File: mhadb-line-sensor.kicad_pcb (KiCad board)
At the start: 2 copper layers, 100 x 20 mm, 106 parts, among them J1 TC2030, J2 Conn_01x04_Pin, J3 Conn_01x04, J4 Conn_01x04_Pin, SW1 SW_Push, SW2 SW_Push, SW3 SW_Push, SW4 SW_Push, U1 HT753-1, U10 QRE1113GR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

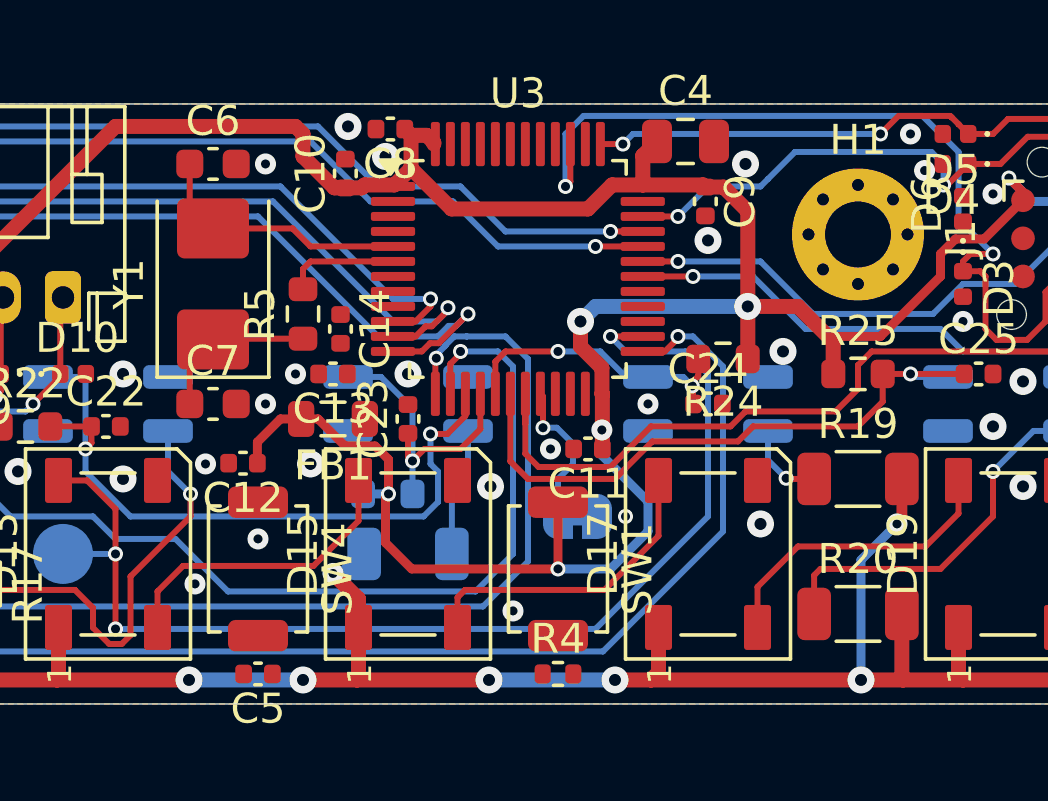
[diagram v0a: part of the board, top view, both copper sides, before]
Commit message: pcb: add BOOT and RST routing
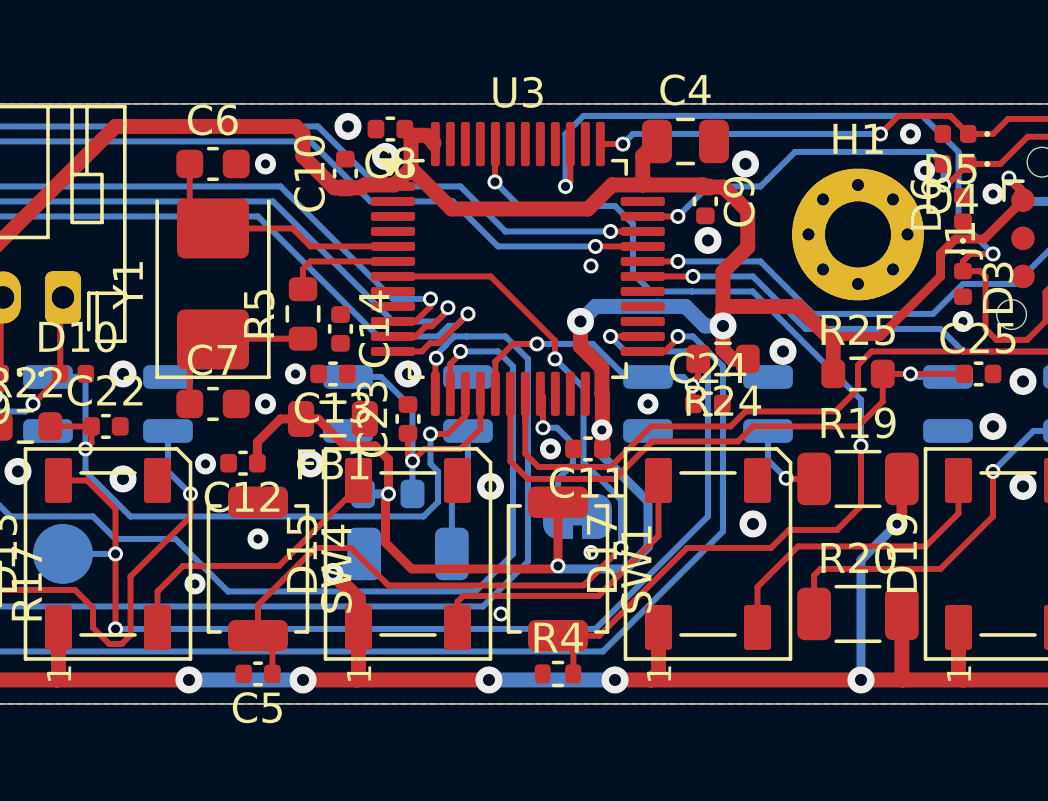
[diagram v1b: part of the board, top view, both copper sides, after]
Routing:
- net /BOOT: track 0.00 -> 34.4 mm, vias 0 -> 2
- net /NRST: track 0.00 -> 30.7 mm, vias 0 -> 2
- net +3V3: track 195.9 -> 198.0 mm
- net Net-(D13-DOUT): track 10.2 -> 9.55 mm
- net GND: vias 65 -> 66

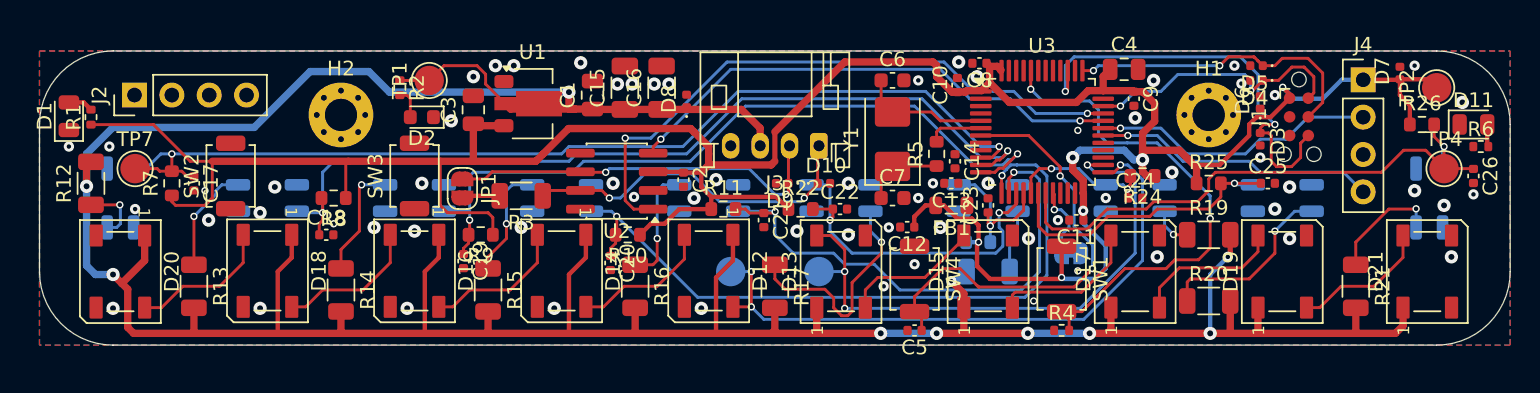
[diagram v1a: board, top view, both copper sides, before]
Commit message: pcb: add tag connect RST and CAN status led routing
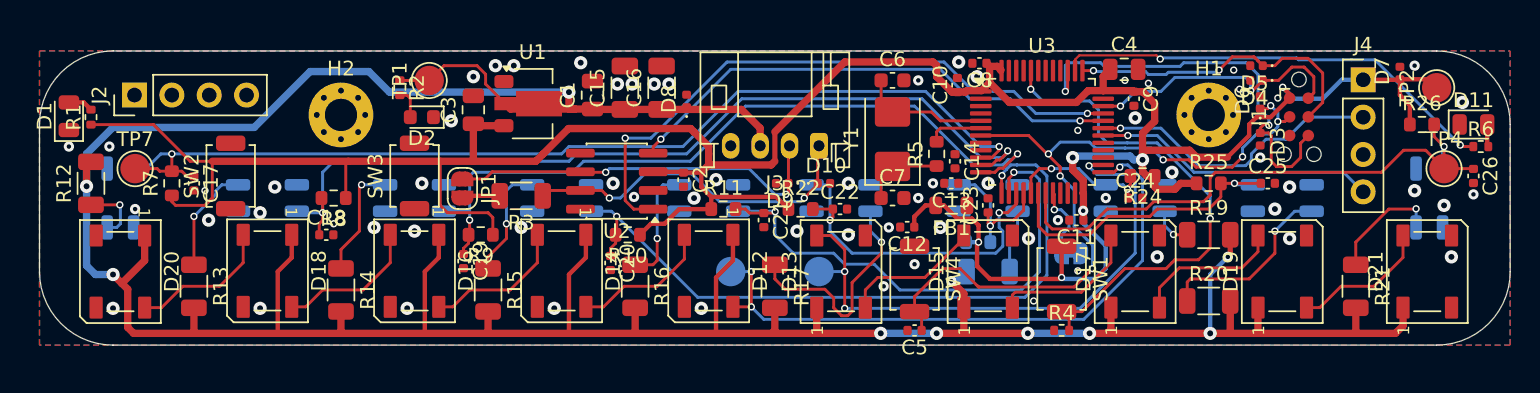
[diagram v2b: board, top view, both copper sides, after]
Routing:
- net Net-(U3-PA15): track 0.00 -> 30.6 mm, vias 0 -> 2
- net /NRST: track 30.7 -> 52.2 mm, vias 2 -> 7
- net +3V3: track 198.0 -> 199.9 mm
- net /U0RXD: track 19.4 -> 20.3 mm
- net /SWO: track 29.1 -> 28.4 mm
- net GND: vias 66 -> 67

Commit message: pcb: add btns routing
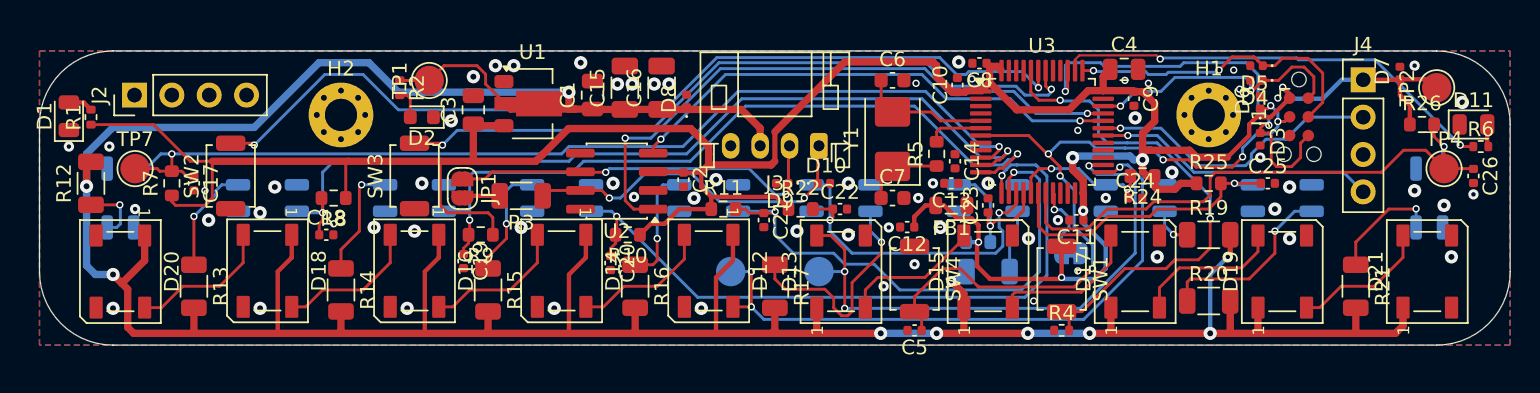
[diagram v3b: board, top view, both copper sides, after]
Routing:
- net /BTN1: track 0.00 -> 61.6 mm, vias 0 -> 2
- net /BTN2: track 0.00 -> 48.4 mm, vias 0 -> 2

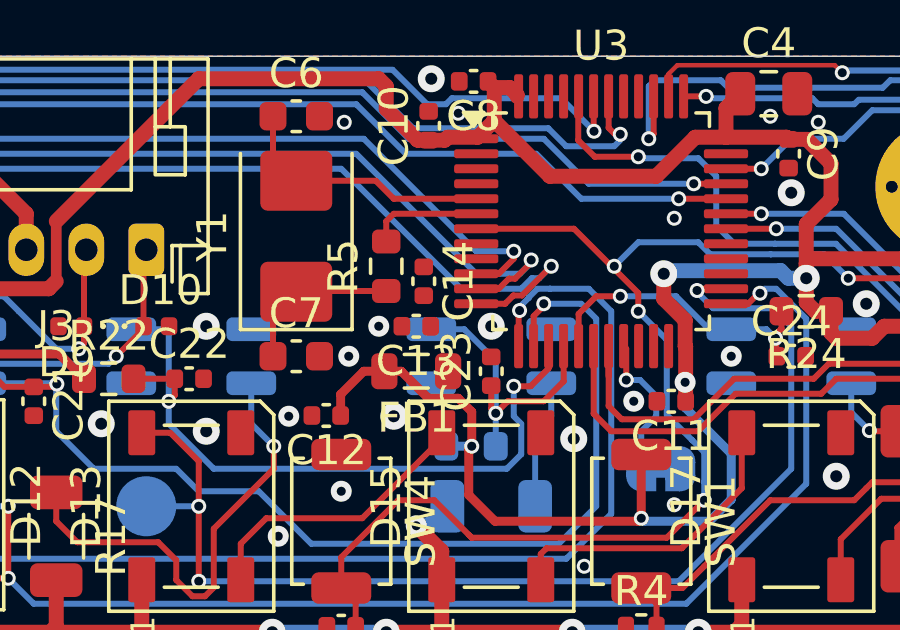
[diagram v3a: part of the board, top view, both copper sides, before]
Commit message: schem/pcb: remove spare GPIOs
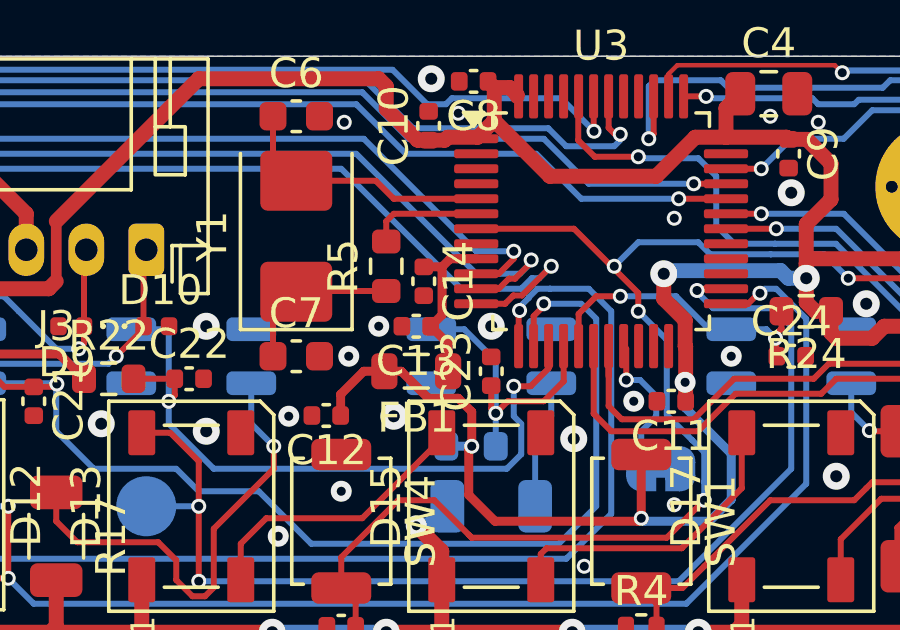
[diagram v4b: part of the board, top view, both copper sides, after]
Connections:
- J2 pad 1: Net-(J2-Pin_1) -> GND
- J2 pad 2: Net-(J2-Pin_2) -> GND
- J2 pad 3: Net-(J2-Pin_3) -> GND
- J2 pad 4: Net-(J2-Pin_4) -> GND
- U3 pad 21: Net-(J2-Pin_3) -> unconnected-(U3-PB10-Pad21)
- U3 pad 22: Net-(J2-Pin_4) -> unconnected-(U3-PB11-Pad22)
- U3 pad 45: Net-(J2-Pin_1) -> unconnected-(U3-PB8-Pad45)
- U3 pad 46: Net-(J2-Pin_2) -> unconnected-(U3-PB9-Pad46)
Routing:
- net Net-(U3-VDDA): track 0.00 -> 5.74 mm

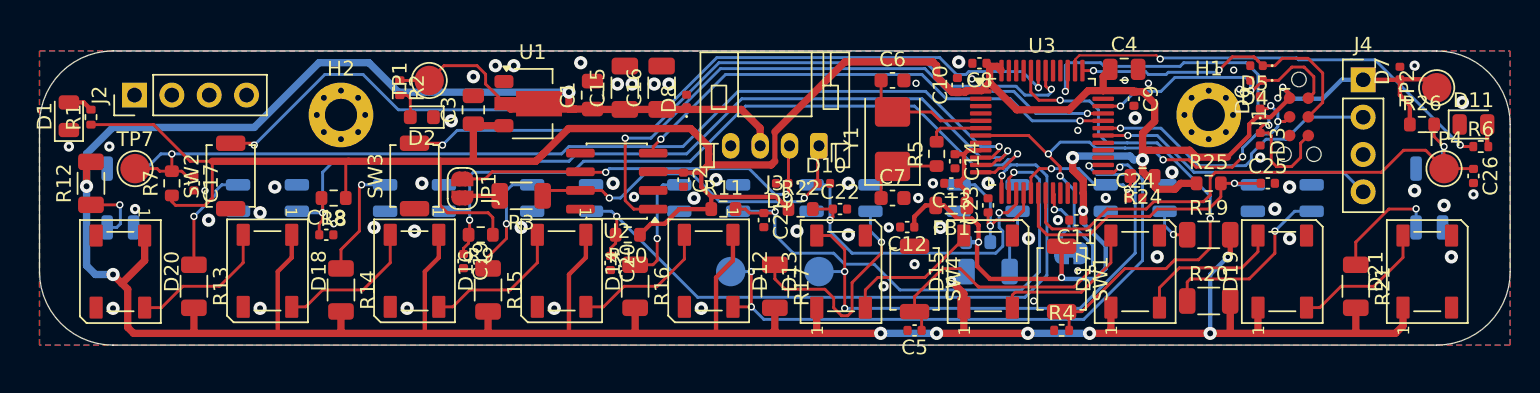
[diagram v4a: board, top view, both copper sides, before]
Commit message: pcb: add stitching vias
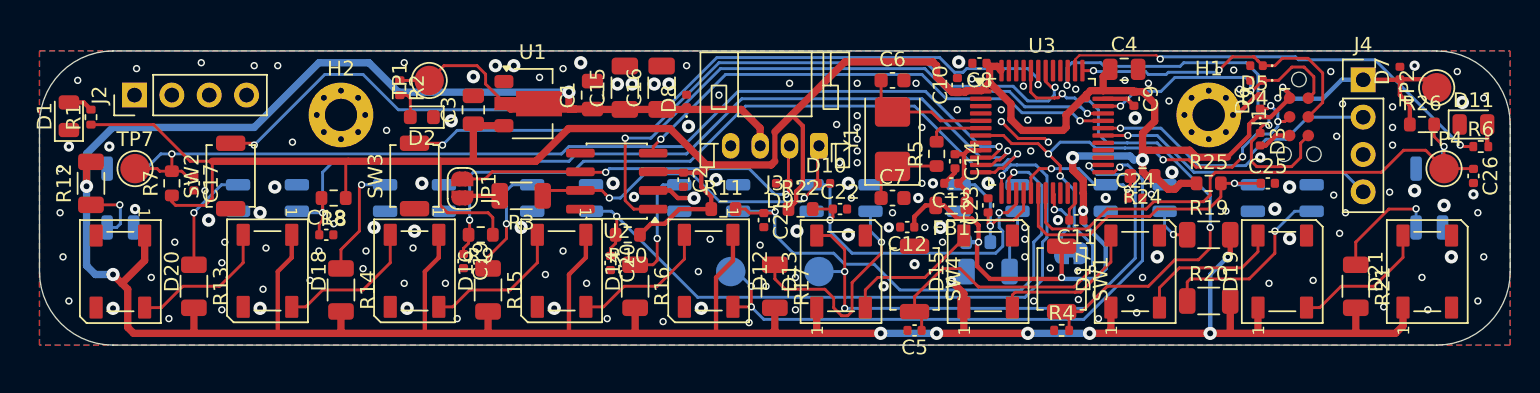
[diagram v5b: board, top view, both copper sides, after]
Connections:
- U3 pad 45: unconnected-(U3-PB8-Pad45) -> GND
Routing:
- net GND: track 0.00 -> 18.7 mm, vias 67 -> 167
- net +3V3: track 200.3 -> 203.1 mm
- net /BTN2: track 48.4 -> 49.2 mm
- net /RGB1: track 42.5 -> 41.9 mm

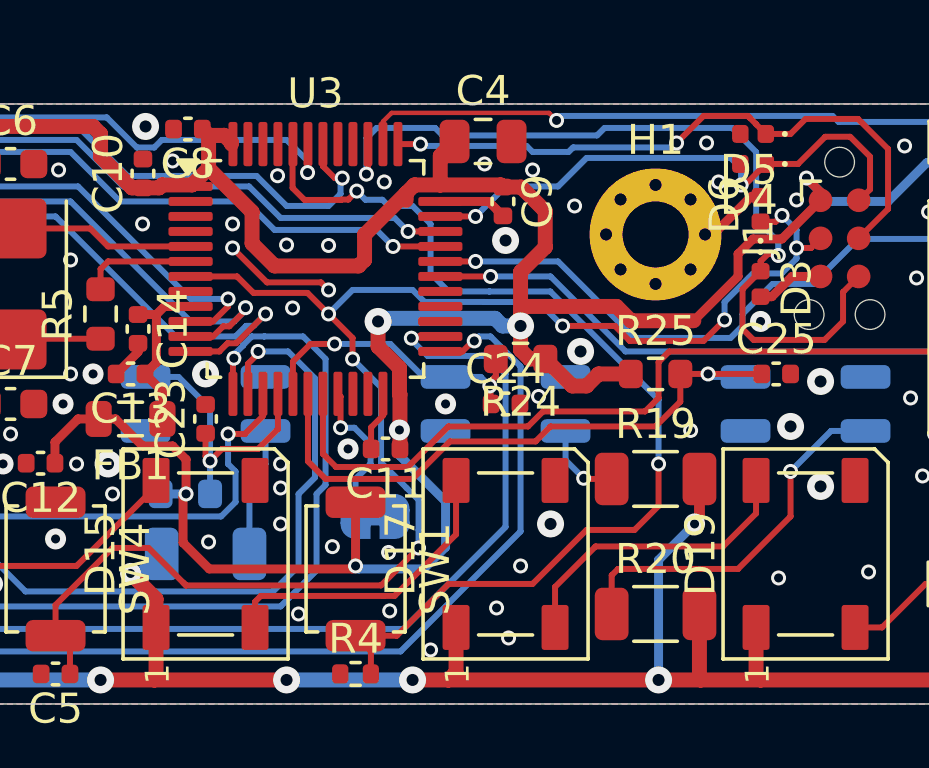
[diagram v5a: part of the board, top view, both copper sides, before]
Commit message: pcb: run and fix DRC
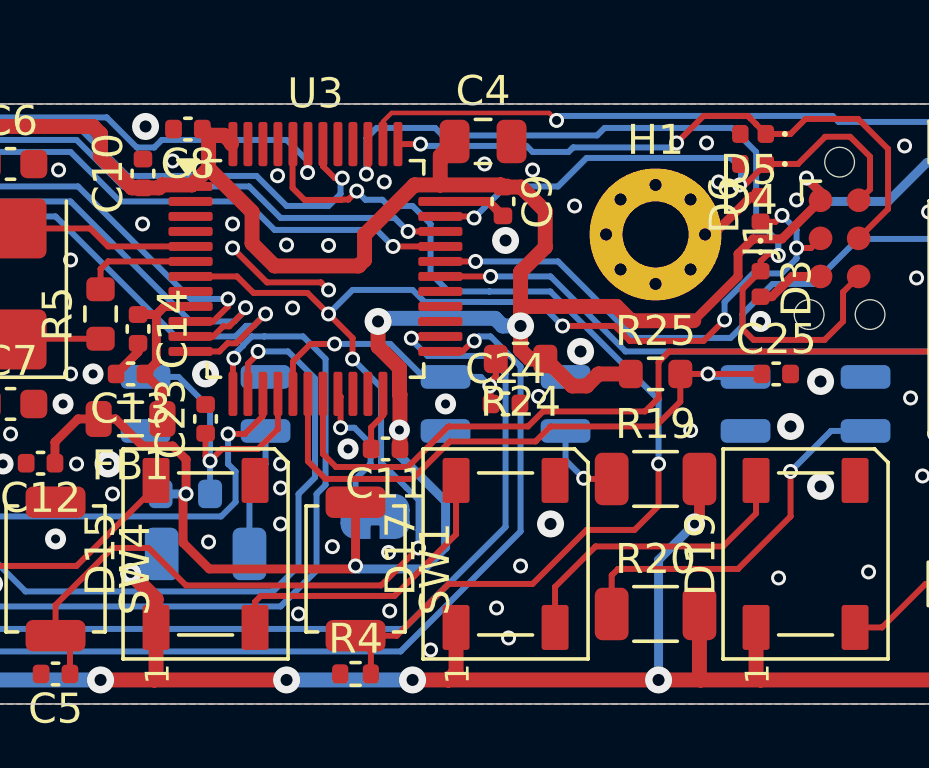
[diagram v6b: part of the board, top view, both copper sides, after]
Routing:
- net /LS10: track 40.5 -> 39.5 mm
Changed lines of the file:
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@@
+	)
+	(segment
+		(start 180.463256 86.699)
+		(end 178.8 88.362256)
+		(width 0.5)
+		(layer "F.Cu")
+		(net 3)
 	)
 	(segment
@@
 	)
 	(segment
-		(start 180.1865 86.975756)
-		(end 178.8 88.362256)
-		(width 0.5)
-		(layer "F.Cu")
-		(net 3)
-	)
-	(segment
-		(start 180.1865 86.975756)
-		(end 180.463256 86.699)
-		(width 0.5)
-		(layer "F.Cu")
-		(net 3)
-	)
-	(segment
 		(start 150.728354 92.215)
 		(end 152.733433 92.215)
@@
 		(end 204 86.5)
 		(width 0.3)
-		(layer "F.Cu")
-		(net 3)
-	)
-	(segment
-		(start 180.1865 87.2135)
-		(end 180.1865 86.975756)
-		(width 0.5)
 		(layer "F.Cu")
 		(net 3)
@@
 	(segment
 		(start 172.849 100.049)
-		(end 172.748 99.948)
+		(end 171.6 98.8)
 		(width 0.2)
 		(layer "F.Cu")
@@
 	)
 	(segment
-		(start 172.849 100.049)
-		(end 171.6 98.8)
-		(width 0.2)
-		(layer "F.Cu")
-		(net 4)
-	)
-	(segment
 		(start 192 87.925)
 		(end 192.507182 87.925)
@@
 	)
 	(segment
-		(start 177.4125 94.6625)
-		(end 177.4125 93.6625)
-		(width 0.2)
-		(layer "F.Cu")
-		(net 17)
-	)
-	(segment
 		(start 177.4125 95.6625)
 		(end 177.4125 93.6625)
@@
 	)
 	(segment
+		(start 182.45 87.8)
+		(end 182.4 87.75)
+		(width 0.2)
+		(layer "F.Cu")
+		(net 21)
+	)
+	(segment
+		(start 192.175 86.003232)
+		(end 192.175 86)
+		(width 0.2)
+		(layer "F.Cu")
+		(net 21)
+	)
+	(segment
+		(start 191.297184 86.7)
+		(end 191.349093 86.7)
+		(width 0.2)
+		(layer "F.Cu")
+		(net 21)
+	)
+	(segment
+		(start 195.649 85.757151)
+		(end 194.985549 85.0937)
+		(width 0.2)
+		(layer "F.Cu")
+		(net 21)
+	)
+	(segment
+		(start 194.985549 85.0937)
+		(end 194.1563 85.0937)
+		(width 0.2)
+		(layer "F.Cu")
+		(net 21)
+	)
+	(segment
+		(start 191.349093 86.7)
+		(end 191.399093 86.75)
+		(width 0.2)
+		(layer "F.Cu")
+		(net 21)
+	)
+	(segment
+		(start 195.27 87.21)
+		(end 195.29 87.21)
+		(width 0.2)
+		(layer "F.Cu")
+		(net 21)
+	)
+	(segment
+		(start 191.399093 86.75)
+		(end 191.428232 86.75)
+		(width 0.2)
+		(layer "F.Cu")
+		(net 21)
+	)
+	(segment
+		(start 195.649 86.851)
+		(end 195.649 85.757151)
+		(width 0.2)
+		(layer "F.Cu")
+		(net 21)
+	)
+	(segment
+		(start 182.4 87.75)
+		(end 181.325 87.75)
+		(width 0.2)
+		(layer "F.Cu")
+		(net 21)
+	)
+	(segment
+		(start 194.1563 85.0937)
+		(end 193.25 86)
+		(width 0.2)
+		(layer "F.Cu")
+		(net 21)
+	)
+	(segment
 		(start 191.428232 86.75)
 		(end 192.175 86.003232)
@@
 	)
 	(segment
-		(start 195.649 85.757151)
-		(end 194.985549 85.0937)
-		(width 0.2)
-		(layer "F.Cu")
-		(net 21)
-	)
-	(segment
-		(start 192.175 86.003232)
-		(end 192.175 86)
-		(width 0.2)
-		(layer "F.Cu")
-		(net 21)
-	)
-	(segment
-		(start 194.985549 85.0937)
-		(end 194.1563 85.0937)
-		(width 0.2)
-		(layer "F.Cu")
-		(net 21)
-	)
-	(segment
-		(start 195.27 87.21)
-		(end 195.29 87.21)
-		(width 0.2)
-		(layer "F.Cu")
-		(net 21)
-	)
-	(segment
-		(start 182.5 87.75)
-		(end 181.325 87.75)
-		(width 0.2)
-		(layer "F.Cu")
-		(net 21)
-	)
-	(segment
-		(start 191.399093 86.75)
-		(end 191.428232 86.75)
-		(width 0.2)
-		(layer "F.Cu")
-		(net 21)
-	)
-	(segment
-		(start 195.649 86.851)
-		(end 195.649 85.757151)
-		(width 0.2)
-		(layer "F.Cu")
-		(net 21)
-	)
-	(segment
-		(start 191.351498 86.702405)
-		(end 191.399093 86.75)
-		(width 0.2)
-		(layer "F.Cu")
-		(net 21)
-	)
-	(segment
-		(start 194.1563 85.0937)
-		(end 193.25 86)
-		(width 0.2)
-		(layer "F.Cu")
-		(net 21)
-	)
-	(segment
 		(start 193.25 86)
 		(end 192.175 86)
@@
 	)
 	(via
-		(at 182.5 87.75)
+		(at 182.45 87.8)
 		(size 0.5)
 		(drill 0.3)
@@
 	)
 	(via
-		(at 191.351498 86.702405)
+		(at 191.297184 86.7)
 		(size 0.5)
 		(drill 0.3)
@@
 	)
 	(segment
+		(start 182.45 87.8)
+		(end 183.5 86.75)
+		(width 0.2)
+		(layer "B.Cu")
+		(net 21)
+	)
+	(segment
+		(start 186.2 85.8)
+		(end 191 85.8)
+		(width 0.2)
+		(layer "B.Cu")
+		(net 21)
+	)
+	(segment
+		(start 185.25 86.75)
+		(end 186.2 85.8)
+		(width 0.2)
+		(layer "B.Cu")
+		(net 21)
+	)
+	(segment
 		(start 191.351498 86.151498)
-		(end 191 85.8)
+		(end 191.351498 86.645686)
 		(width 0.2)
 		(layer "B.Cu")
@@
 	)
 	(segment
+		(start 191.351498 86.645686)
+		(end 191.297184 86.7)
+		(width 0.2)
+		(layer "B.Cu")
+		(net 21)
+	)
+	(segment
 		(start 183.5 86.75)
-		(end 182.5 87.75)
+		(end 185.25 86.75)
 		(width 0.2)
 		(layer "B.Cu")
@@
 	(segment
 		(start 191 85.8)
-		(end 186.2 85.8)
-		(width 0.2)
-		(layer "B.Cu")
-		(net 21)
-	)
-	(segment
-		(start 191.351498 86.702405)
 		(end 191.351498 86.151498)
 		(width 0.2)
 		(layer "B.Cu")
-		(net 21)
-	)
-	(segment
-		(start 185.25 86.75)
-		(end 183.5 86.75)
-		(width 0.2)
-		(layer "B.Cu")
-		(net 21)
-	)
-	(segment
-		(start 186.2 85.8)
-		(end 185.25 86.75)
-		(width 0.2)
-		(layer "B.Cu")
